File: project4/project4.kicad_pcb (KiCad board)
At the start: 2 copper layers, 21 parts, among them J1 Conn_02x07_Row_Letter_First, U1 SST27ST020, U2 SST27ST020, U3 74LS02, U4 74LS670, U5 74LS139, U6 74LS670

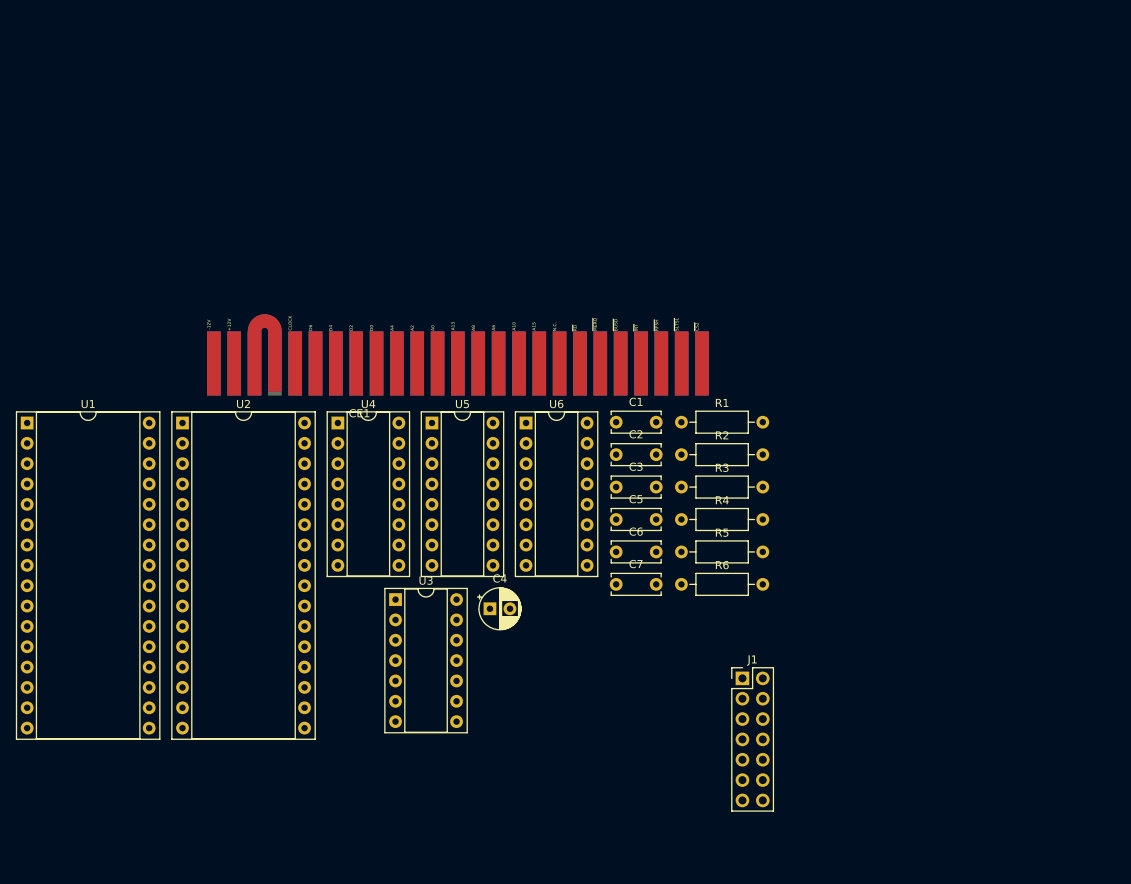
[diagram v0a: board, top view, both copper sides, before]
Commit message: Modify PCB4
Signed-off-by: Youngki Park <ykp7409@gmail.com>
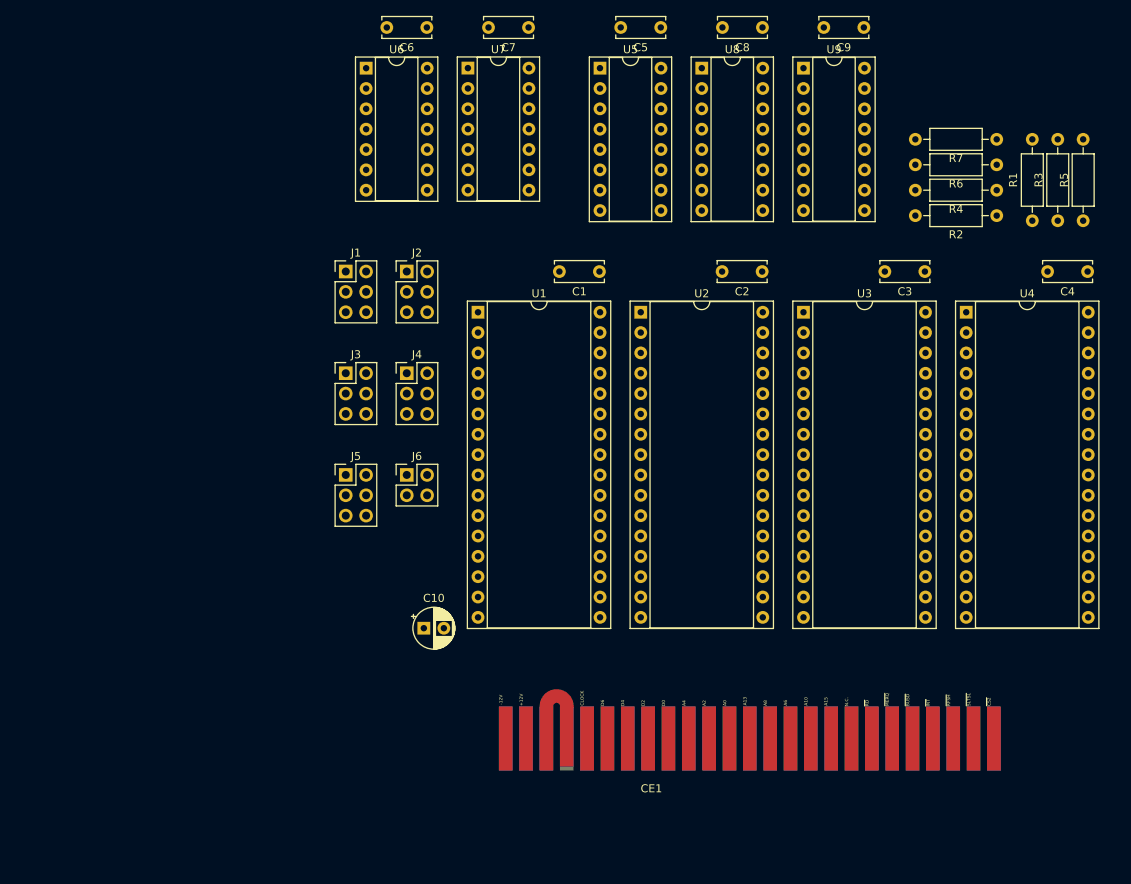
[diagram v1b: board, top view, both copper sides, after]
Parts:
- added C10: 10uF, Capacitor_THT:CP_Radial_D5.0mm_P2.50mm, F.Cu at (105.0, 123.3)
- added C8: 0.1uF, Capacitor_THT:C_Disc_D6.0mm_W2.5mm_P5.00mm, F.Cu at (147.3, 48.3)
- added C9: 0.1uF, Capacitor_THT:C_Disc_D6.0mm_W2.5mm_P5.00mm, F.Cu at (159.9, 48.3)
- added J2: Conn_02x03_Odd_Even, Connector_PinHeader_2.54mm:PinHeader_2x03_P2.54mm_Vertical, F.Cu at (102.9, 78.7)
- added J3: Conn_02x03_Odd_Even, Connector_PinHeader_2.54mm:PinHeader_2x03_P2.54mm_Vertical, F.Cu at (95.2, 91.4)
- added J4: Conn_02x03_Odd_Even, Connector_PinHeader_2.54mm:PinHeader_2x03_P2.54mm_Vertical, F.Cu at (102.9, 91.4)
- added J5: Conn_02x03_Odd_Even, Connector_PinHeader_2.54mm:PinHeader_2x03_P2.54mm_Vertical, F.Cu at (95.2, 104.1)
- added J6: Conn_02x02_Odd_Even, Connector_PinHeader_2.54mm:PinHeader_2x02_P2.54mm_Vertical, F.Cu at (102.9, 104.1)
- added R7: 470, Resistor_THT:R_Axial_DIN0207_L6.3mm_D2.5mm_P10.16mm_Horizontal, F.Cu at (176.5, 62.2)
- added U7: 74LS00, Package_DIP:DIP-14_W7.62mm_Socket, F.Cu at (110.5, 53.3)
- added U8: 74LS670, Package_DIP:DIP-16_W7.62mm_Socket, F.Cu at (139.7, 53.3)
- added U9: 74LS670, Package_DIP:DIP-16_W7.62mm_Socket, F.Cu at (152.4, 53.3)
- C4: value 10uF -> 0.1uF; footprint Capacitor_THT:CP_Radial_D5.0mm_P2.50mm -> Capacitor_THT:C_Disc_D6.0mm_W2.5mm_P5.00mm
- J1: value Conn_02x07_Row_Letter_First -> Conn_02x03_Odd_Even; footprint Connector_PinHeader_2.54mm:PinHeader_2x07_P2.54mm_Vertical -> Connector_PinHeader_2.54mm:PinHeader_2x03_P2.54mm_Vertical
- U3: value 74LS02 -> SST27ST020; footprint Package_DIP:DIP-14_W7.62mm_Socket -> Package_DIP:DIP-32_W15.24mm_Socket
- U4: value 74LS670 -> SST27ST020; footprint Package_DIP:DIP-16_W7.62mm_Socket -> Package_DIP:DIP-32_W15.24mm_Socket
- U6: value 74LS670 -> 74LS32; footprint Package_DIP:DIP-16_W7.62mm_Socket -> Package_DIP:DIP-14_W7.62mm_Socket
- moved C4 85.7 mm to (187.9, 78.7), turned to 180 degrees
- moved U4 79.7 mm to (172.7, 83.8)
- moved J1 71.0 mm to (95.2, 78.7)
- moved C7 70.4 mm to (118.1, 48.3), turned to 180 degrees
- moved C6 69.6 mm to (105.4, 48.3), turned to 180 degrees
- moved R6 65.5 mm to (176.5, 65.4), turned to 180 degrees
- moved R5 65.0 mm to (187.3, 72.4), turned to 90 degrees
- moved U3 62.3 mm to (152.4, 83.8)
- moved C5 61.7 mm to (134.6, 48.3), turned to 180 degrees
- moved CE1 59.3 mm to (144.4, 133.9)
- moved U2 58.9 mm to (132.1, 83.8)
- moved U1 58.0 mm to (111.8, 83.8)
- moved R3 57.6 mm to (184.2, 72.4), turned to 90 degrees
- moved R4 56.9 mm to (176.5, 68.6), turned to 180 degrees
- moved R1 50.5 mm to (181.0, 72.4), turned to 90 degrees
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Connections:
- CE1 pad 25: unconnected-(CE1-A14-Pad25) -> /A14
- J1 pad 1: (no net) -> /A15
- J1 pad 2: (no net) -> Net-(J1-Pin_2)
- J1 pad 3: (no net) -> /A11
- J1 pad 4: (no net) -> Net-(J1-Pin_2)
- J1 pad 5: (no net) -> /A12
- J1 pad 6: (no net) -> Net-(J1-Pin_2)
- R1 pad 2: /MA13 -> Net-(U5A-A0)
- R2 pad 2: /MA14 -> /MA16
- R3 pad 2: /MA15 -> /MA17
- R4 pad 2: /MA16 -> /MA15
- R5 pad 2: Net-(U5A-A0) -> Net-(U5A-A1)
- R6 pad 2: /MA17 -> /MA14
- U3 pad 1: Net-(U3-Pad1) -> +5V
- U3 pad 10: Net-(U4-~{Er}) -> /A2
- U3 pad 11: (no net) -> /A1
- U3 pad 12: (no net) -> /A0
- U3 pad 13: (no net) -> /D0
- U3 pad 14: +5V -> /D1
- U3 pad 2: //WR -> /MA16
- U3 pad 3: //SLTSL -> /MA15
- U3 pad 4: Net-(U4-~{Ew}) -> /A12
- U3 pad 5: Net-(U3-Pad1) -> /A7
- U3 pad 6: Net-(U3-Pad1) -> /A6
- U3 pad 7: GND -> /A5
- U3 pad 8: unconnected-(U3-Pad8) -> /A4
- U3 pad 9: unconnected-(U3-Pad9) -> /A3
- U4 pad 1: /D2 -> +5V
- U4 pad 10: /MA16 -> /A2
- U4 pad 11: Net-(U4-~{Er}) -> /A1
- U4 pad 12: Net-(U4-~{Ew}) -> /A0
- U4 pad 13: /A11 -> /D0
- U4 pad 14: /A12 -> /D1
- U4 pad 15: /D3 -> /D2
- U4 pad 16: +5V -> GND
- U4 pad 2: /D1 -> /MA16
- U4 pad 3: /D0 -> /MA15
- U4 pad 4: /A13 -> /A12
- U4 pad 5: /A15 -> /A7
- U4 pad 6: /MA13 -> /A6
- U4 pad 7: /MA14 -> /A5
- U4 pad 8: GND -> /A4
- U4 pad 9: /MA15 -> /A3
- U5 pad 3: GND -> Net-(U5A-A1)
- U5 pad 6: unconnected-(U5A-O2-Pad6) -> /ROM_CE3
- U5 pad 7: unconnected-(U5A-O3-Pad7) -> /ROM_CE4
- U6 pad 1: /D5 -> //WR
- U6 pad 10: /MA17 -> Net-(U6-Pad10)
- U6 pad 11: Net-(U4-~{Er}) -> Net-(U6-Pad11)
- U6 pad 12: Net-(U4-~{Ew}) -> /A15
- U6 pad 13: /A11 -> /A13
- U6 pad 14: /A12 -> +5V
- U6 pad 2: unconnected-(U6-D3-Pad2) -> //SLTSL
- U6 pad 3: unconnected-(U6-D4-Pad3) -> Net-(U6-Pad3)
- U6 pad 4: /A13 -> Net-(U6-Pad4)
- U6 pad 5: /A15 -> Net-(U6-Pad3)
- U6 pad 6: unconnected-(U6-Q4-Pad6) -> Net-(U8-~{Ew})
- U6 pad 7: unconnected-(U6-Q3-Pad7) -> GND
- U6 pad 8: GND -> Net-(U6-Pad4)
- U6 pad 9: Net-(U5A-A0) -> Net-(J1-Pin_2)

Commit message: Modified PCB 4
Signed-off-by: ykp74 <ykp7409@gmail.com>
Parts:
- J1, J2, J3, J4, J5: value Conn_02x03_Odd_Even -> Conn_02x03
- J6: value Conn_02x02_Odd_Even -> Conn_02x02
- moved J2 23.4 mm to (94.0, 100.3)
- moved J4 23.4 mm to (94.0, 113.0)
- moved J6 16.5 mm to (102.9, 87.6)
- moved C9 13.1 mm to (165.1, 60.3)
- moved C6 13.1 mm to (110.5, 60.3)
- moved C7 13.1 mm to (123.2, 60.3)
- moved C8 13.1 mm to (152.4, 60.3)
- moved C5 13.1 mm to (139.7, 60.3)
- moved J3 11.7 mm to (102.9, 100.3)
- moved J5 11.7 mm to (102.9, 113.0)
- moved U8 11.4 mm to (144.8, 63.5)
- moved R5 11.4 mm to (182.2, 62.2), turned to 180 degrees
- moved U5 11.4 mm to (132.1, 63.5)
- moved U6 11.4 mm to (102.9, 63.5)
- moved U7 11.4 mm to (115.6, 63.5)
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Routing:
- net +5V: track 0.00 -> 422.0 mm, vias 0 -> 1
- net /A15: track 0.00 -> 216.5 mm, vias 0 -> 1
- net /A13: track 0.00 -> 201.8 mm, vias 0 -> 1
- net //WR: track 0.00 -> 182.3 mm
- net /A11: track 0.00 -> 172.7 mm
- net //SLTSL: track 0.00 -> 169.4 mm, vias 0 -> 1
- net /A12: track 0.00 -> 164.2 mm
- net /D5: track 0.00 -> 157.7 mm
- net /D6: track 0.00 -> 153.8 mm, vias 0 -> 1
- net /D4: track 0.00 -> 150.6 mm, vias 0 -> 1
- net /D1: track 0.00 -> 150.3 mm
- net /D2: track 0.00 -> 148.1 mm, vias 0 -> 1
- net /D0: track 0.00 -> 148.0 mm, vias 0 -> 1
- net /D3: track 0.00 -> 145.6 mm
- net /MA16: track 0.00 -> 129.8 mm, vias 0 -> 1
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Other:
- board outline added: 100.8 x 98.2 mm

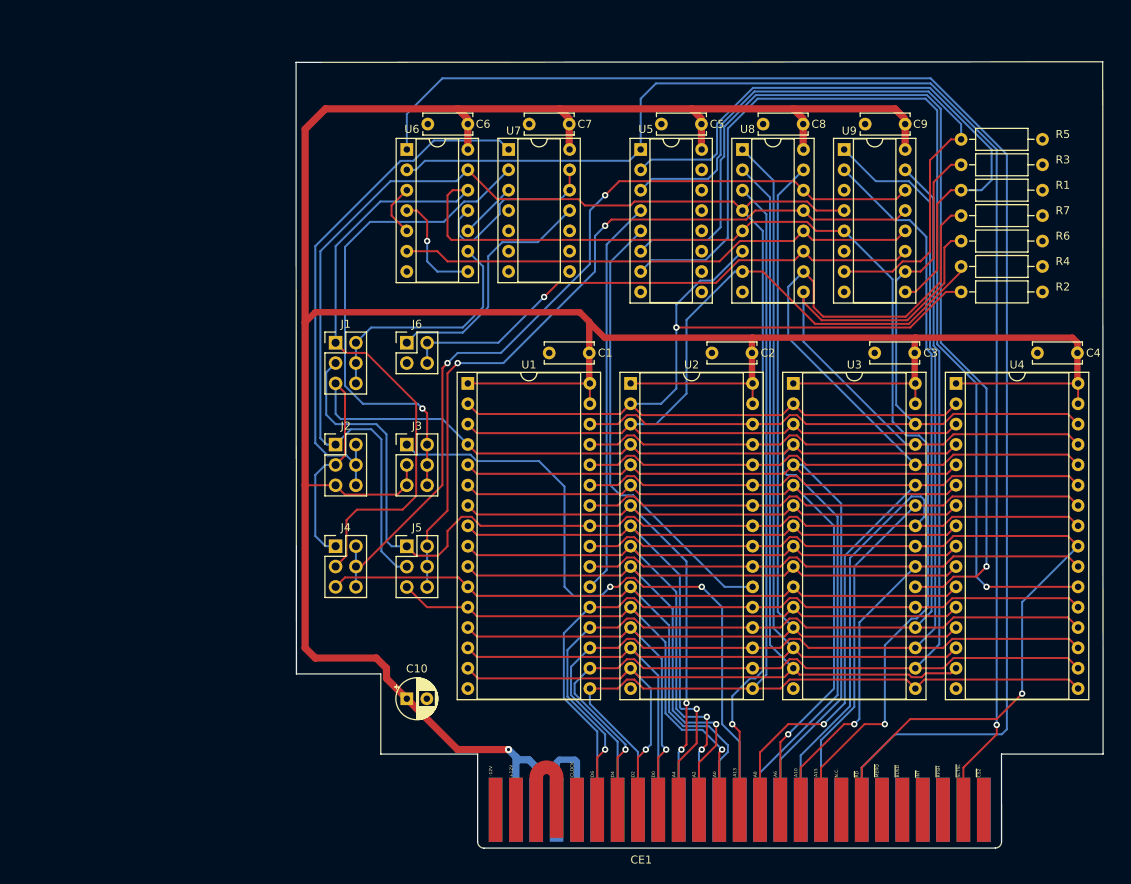
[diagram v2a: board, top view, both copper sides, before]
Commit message: Modify PCB4
Signed-off-by: Youngki Park <ykp7409@gmail.com>
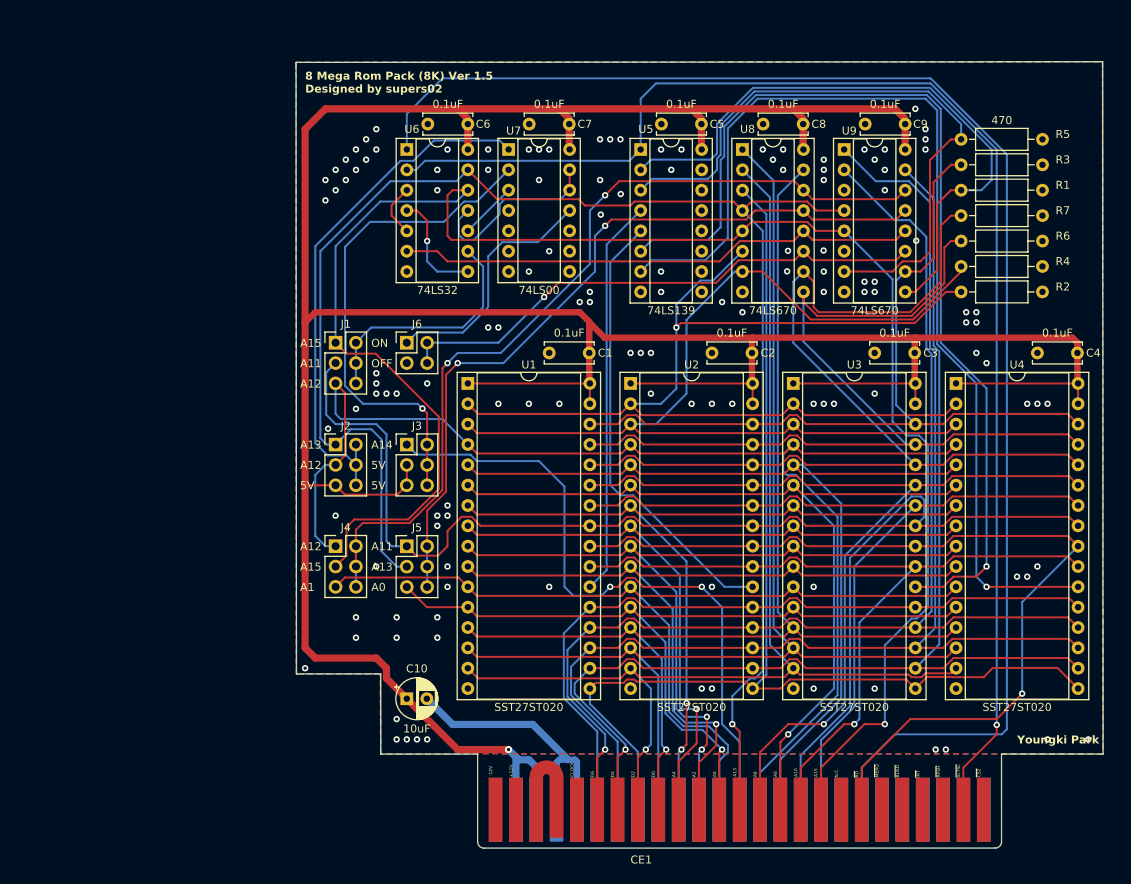
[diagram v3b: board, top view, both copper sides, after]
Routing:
- net GND: track 14.7 -> 35.5 mm, vias 0 -> 132
- net /A15: track 216.5 -> 220.1 mm
- net Net-(J4-Pin_2): track 107.5 -> 110.5 mm
- net /D3: track 145.6 -> 146.8 mm
- net /MA13: track 128.6 -> 127.6 mm
- added copper zone on B.Cu, net GND
- added copper zone on F.Cu, net GND
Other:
- board text added: "5V"
- board text added: "8 Mega Rom Pack (8K) Ver 1.5 Designed by supers02"
- board text added: "A0"
- board text added: "A1"
- board text added: "A11"
- board text added: "A12"
- board text added: "A13"
- board text added: "A14"
- board text added: "A15"
- board text added: "OFF"
- board text added: "ON"
- board text added: "Youngki Park"
